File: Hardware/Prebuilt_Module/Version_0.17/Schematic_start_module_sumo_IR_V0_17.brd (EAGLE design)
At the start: 10.4 x 11.4 mm, 20 parts, among them IC1 ATTINY24,44,84_QFNVQFN

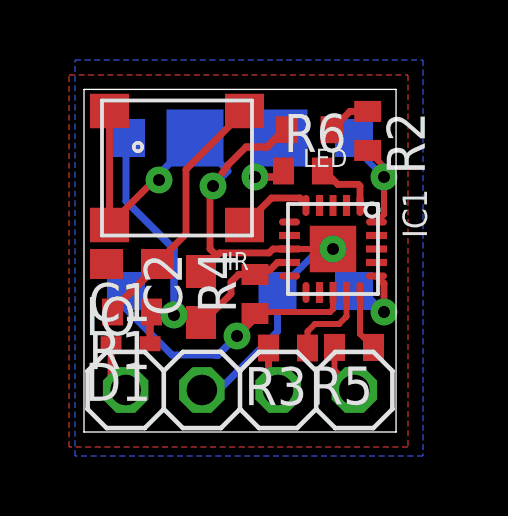
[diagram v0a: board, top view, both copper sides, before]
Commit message: Version 0.17
Since it was not very expensive to get the manufacturer to flip the
IR-receiver, it's best to go with a version similar to the old one
(V0.16). What is new from that verison is a new microcontroller
(Attiny44A), anothe LED and resistors in 0402.
Furthermore, the version with another IR-receiver (V1.0) has been
slightly updated.
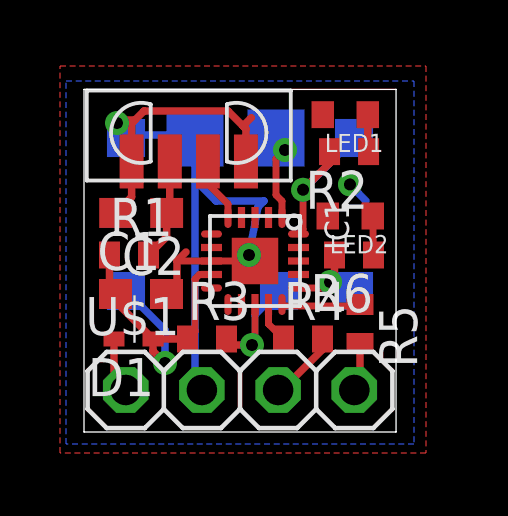
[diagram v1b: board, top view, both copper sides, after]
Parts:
- removed IR: TSOP85AP, CRF:TSOP85AP
- removed LED: (no value), CRF:0603_SMALL
- added IR1: TSOP77338TS, CRF:TSOP77338
- added LED1: green, CRF:0603_SMALL
- added LED2: red, CRF:0603_SMALL
- C1: value 1uF -> 100nF
- MISO_PAD: value mosi -> (none)
- R2: value 470R -> 470
- R3: value 1k -> 1K
- R6: value 1k -> 470
- SCK_PAD: value (none) -> mosi
- moved GND_PAD 7.18 mm to (1.40, 9.80)
- moved VCC_PAD 5.10 mm to (1.40, 4.70)
- moved RESET_PAD 5.10 mm to (6.50, 4.70), turned to 180 degrees
- moved R6 3.28 mm to (9.00, 5.90), turned to 180 degrees
- moved R3 2.72 mm to (4.10, 3.10), turned to 0 degrees
- moved IC1 2.63 mm to (5.70, 5.70)
- moved R4 2.19 mm to (7.30, 3.10), turned to 0 degrees
- moved C2 2.00 mm to (1.90, 4.60), turned to 0 degrees
- moved R1 1.90 mm to (1.50, 5.90), turned to 0 degrees
- moved C1 1.73 mm to (1.91, 7.30)
- moved R2 0.93 mm to (8.84, 9.34), turned to 180 degrees
- moved R5 0.81 mm to (9.20, 3.60), turned to 270 degrees
- moved D1 0.19 mm to (1.70, 3.10)
- moved SCK_PAD 0.10 mm to (6.40, 9.80), turned to 90 degrees
- renumbered IO to U$1
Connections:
- net KILL_SWITCH renamed N$4
- removed net N$6: C1.1, IR.4, R1.2
- removed net START_SIGNAL: R3.2, U$1.3
- new net N$3: LED1.1, R2.1
- new net N$5: R4.2, U$1.3
- net GND: now also IR1.1, IR1.4, LED1.2, LED2.2; no longer IR.1, IR.2, LED.2
- net IR: now also IR1.3; no longer IR.3
- net MOSI: now also R6.2
- net N$1: now also LED2.1, R6.1; no longer LED.1, R2.1
- net N$2: now also C1.1, IR1.2, R1.2; no longer R6.1, SCK_PAD.P$1
- net RESET: now also R3.2; no longer R4.1
- net SCK: now also SCK_PAD.P$1; no longer R6.2
- net START: now also R4.1; no longer R3.1
- net VCC: now also R3.1; no longer R4.2
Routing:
- net N$6: track 8.52 -> 0.00 mm
- net RESET: track 9.53 -> 4.80 mm
- net GND: track 27.8 -> 31.2 mm
- net N$5: track 0.00 -> 2.39 mm
- net VCC: track 13.4 -> 11.2 mm
- net N$3: track 0.00 -> 1.80 mm
- net MISO: track 4.43 -> 6.16 mm
- net START_SIGNAL: track 1.53 -> 0.00 mm
- net START: track 2.86 -> 1.36 mm
- net SCK: track 2.11 -> 2.96 mm, vias 0 -> 1
- net N$2: track 2.66 -> 3.41 mm, vias 1 -> 0
- net KILL: track 2.02 -> 2.63 mm
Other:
- board text removed: "KILL"
- board text removed: "START"
